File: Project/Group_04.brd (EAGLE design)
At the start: 71.1 x 58.4 mm, 29 parts, among them J1 POWER_JACKPTH_LOCK, U1 +12v

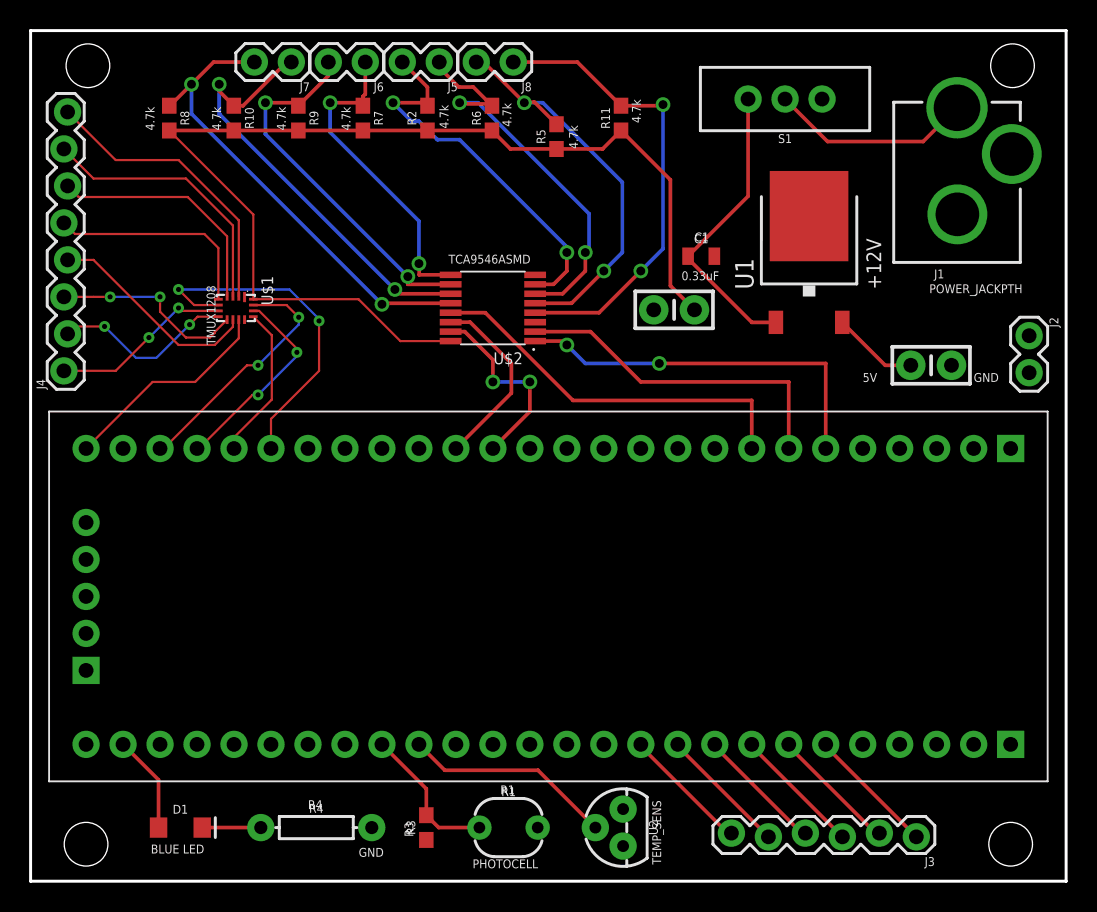
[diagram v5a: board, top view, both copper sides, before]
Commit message: copper pour modified, power jack re-oriented
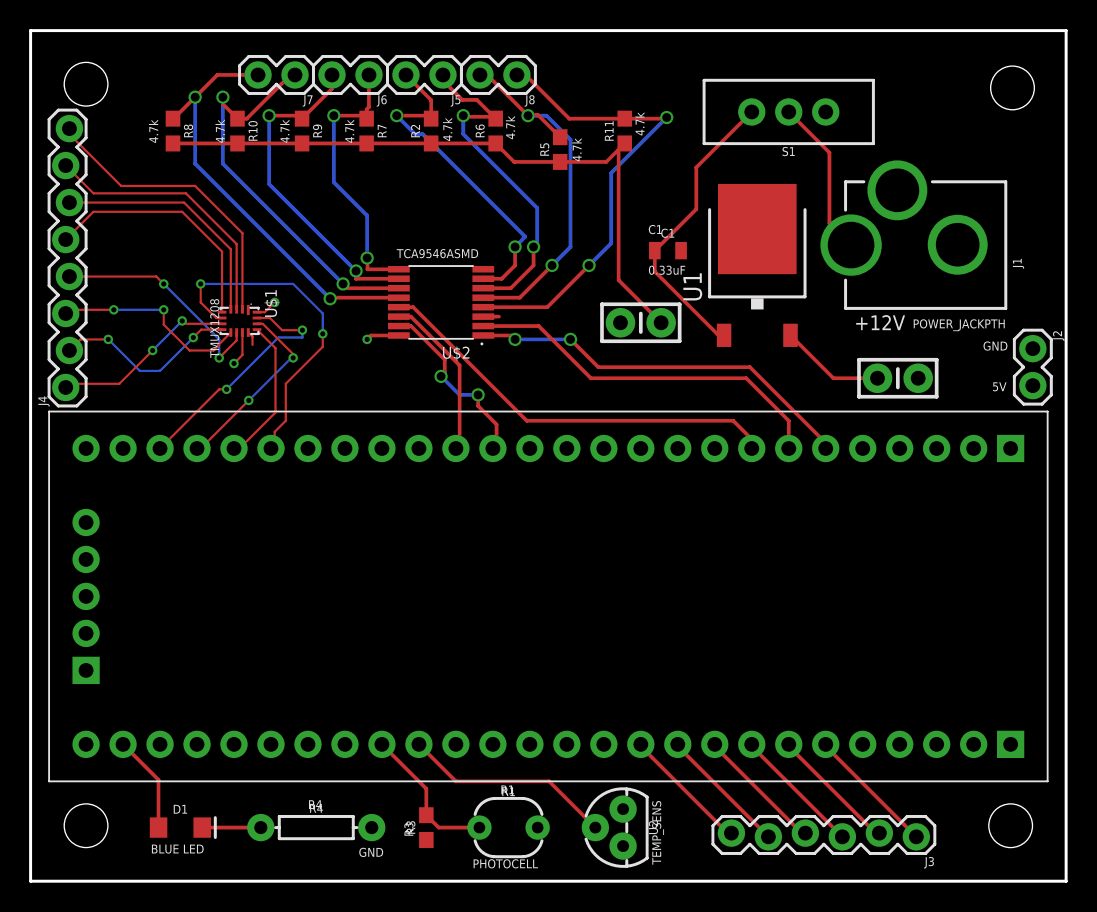
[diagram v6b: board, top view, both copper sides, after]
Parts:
- moved J1 7.96 mm to (70.2, 43.7), turned to 90 degrees
- moved U1 3.67 mm to (49.9, 42.3)
- moved U$2 3.58 mm to (28.2, 39.8)
- moved C2 2.45 mm to (41.9, 38.4)
- moved C3 2.45 mm to (59.6, 34.5)
- moved C1 2.32 mm to (43.8, 43.3)
- moved J4 1.15 mm to (2.54, 33.9)
- moved J2 0.92 mm to (68.8, 36.6)
- moved J8 0.92 mm to (33.4, 55.4)
- moved J5 0.92 mm to (28.3, 55.4)
- moved J6 0.92 mm to (23.2, 55.4)
- moved J7 0.92 mm to (18.2, 55.4)
- moved R2 0.92 mm to (27.5, 51.5)
- moved R6 0.92 mm to (31.9, 51.5)
- moved R10 0.92 mm to (14.2, 51.5)
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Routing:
- net 5V: track 96.0 -> 59.2 mm, vias 0 -> 3
- net I2C_SDA_1: track 27.6 -> 24.0 mm
- net I2C_SCL_1: track 26.4 -> 23.3 mm
- net N$1: track 14.0 -> 10.9 mm
- net I2C_SDA_3: track 30.3 -> 27.5 mm
- net I2C_SCL_0: track 28.6 -> 25.7 mm
- net I2C_SCL_3: track 32.5 -> 29.7 mm
- net I2C_SCL_2: track 25.7 -> 22.8 mm
- net I2C_SDA_2: track 22.0 -> 19.1 mm
- net I2C_A1: track 23.4 -> 25.6 mm
- net I2C_A2: track 26.5 -> 28.6 mm
- net GND: track 0.00 -> 2.05 mm
- net N$13: track 14.8 -> 16.8 mm
- net I2C_SCL: track 12.8 -> 11.4 mm
- net MUX_A1: track 14.1 -> 12.8 mm
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
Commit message: adjusted wire warning
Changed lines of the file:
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@@
 <wire x1="14.986" y1="33.02" x2="11.684" y2="29.718" width="0.1524" layer="1"/>
 <via x="14.986" y="33.02" extent="1-16" drill="0.35"/>
-<wire x1="17.907" y1="35.941" x2="18.034" y2="35.941" width="0.1524" layer="16"/>
-<wire x1="17.907" y1="35.941" x2="14.986" y2="33.02" width="0.1524" layer="16"/>
 <via x="18.034" y="35.941" extent="1-16" drill="0.35"/>
 <wire x1="18.034" y1="35.941" x2="18.034" y2="36.195" width="0.1524" layer="1"/>
 <wire x1="18.034" y1="36.195" x2="15.948" y2="38.281" width="0.1524" layer="1"/>
-<wire x1="14.986" y1="33.02" x2="18.034" y2="35.941" width="0" layer="19"/>
+<wire x1="14.986" y1="33.02" x2="17.907" y2="35.941" width="0.1524" layer="16"/>
+<wire x1="17.907" y1="35.941" x2="18.034" y2="35.941" width="0.1524" layer="16"/>
 </signal>
 <signal name="MUX_A0">
